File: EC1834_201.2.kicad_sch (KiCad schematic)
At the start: 69 parts, among them X4 Lautsprecher, X7 DB9_Female

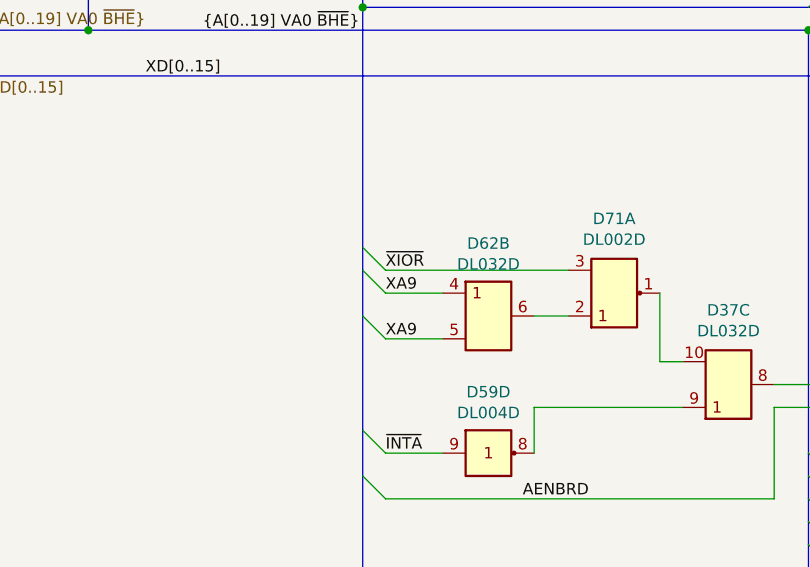
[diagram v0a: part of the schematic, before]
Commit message: Wrong Signal fixed
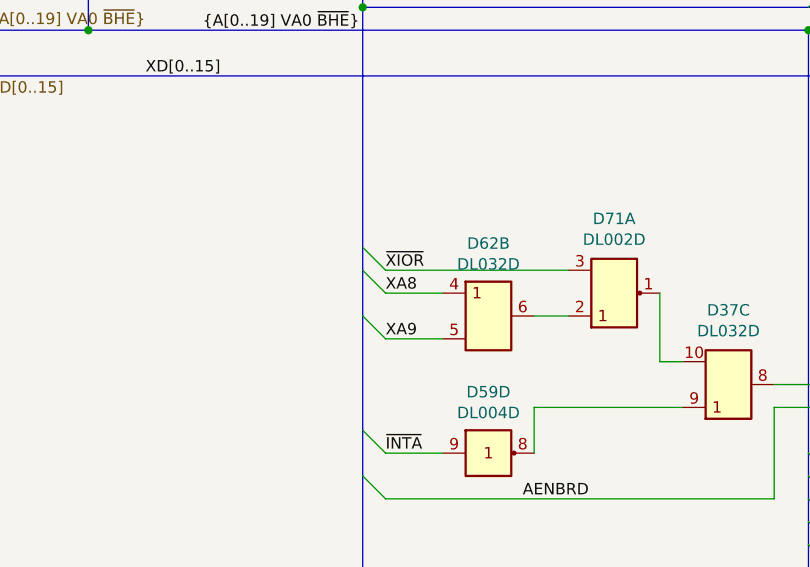
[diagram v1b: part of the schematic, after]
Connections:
- net XA8: now also D62.4 (A2)
- net XA9: no longer D62.4 (A2)
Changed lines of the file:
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@@
     (effects (font (size 1.27 1.27)) (justify left bottom))
   )
-  (label "XA9" (at 87.63 218.44 0)
+  (label "XA8" (at 87.63 218.44 0)
     (effects (font (size 1.27 1.27)) (justify left bottom))
   )

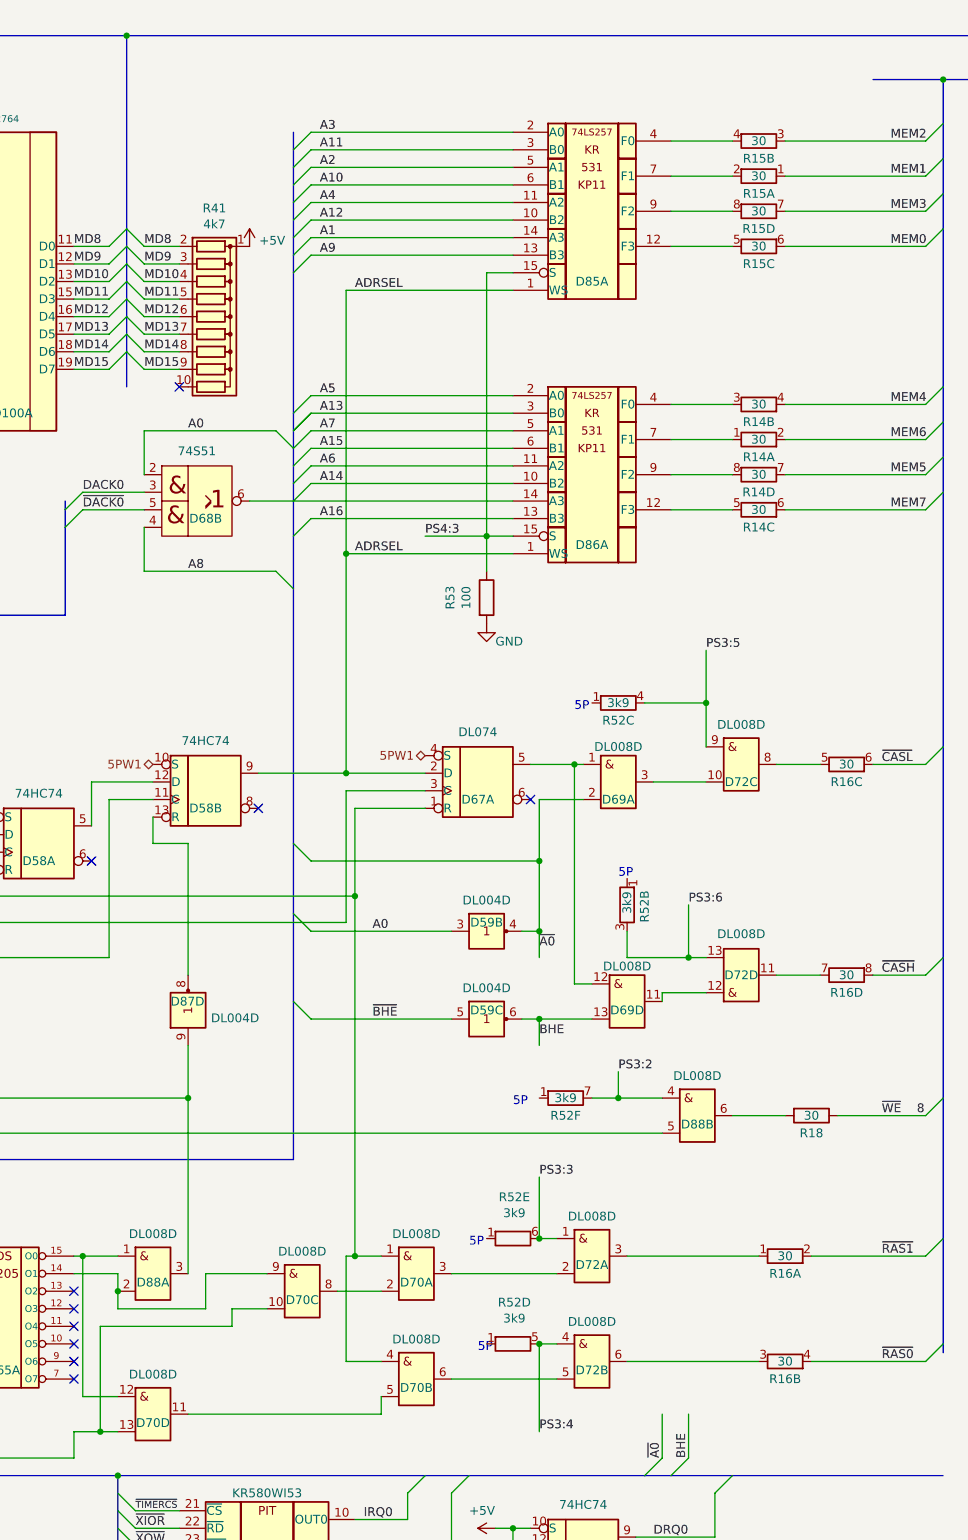
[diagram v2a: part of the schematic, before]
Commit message: Replaced/corrected D70 from DL008 with DL000 Updated schematics
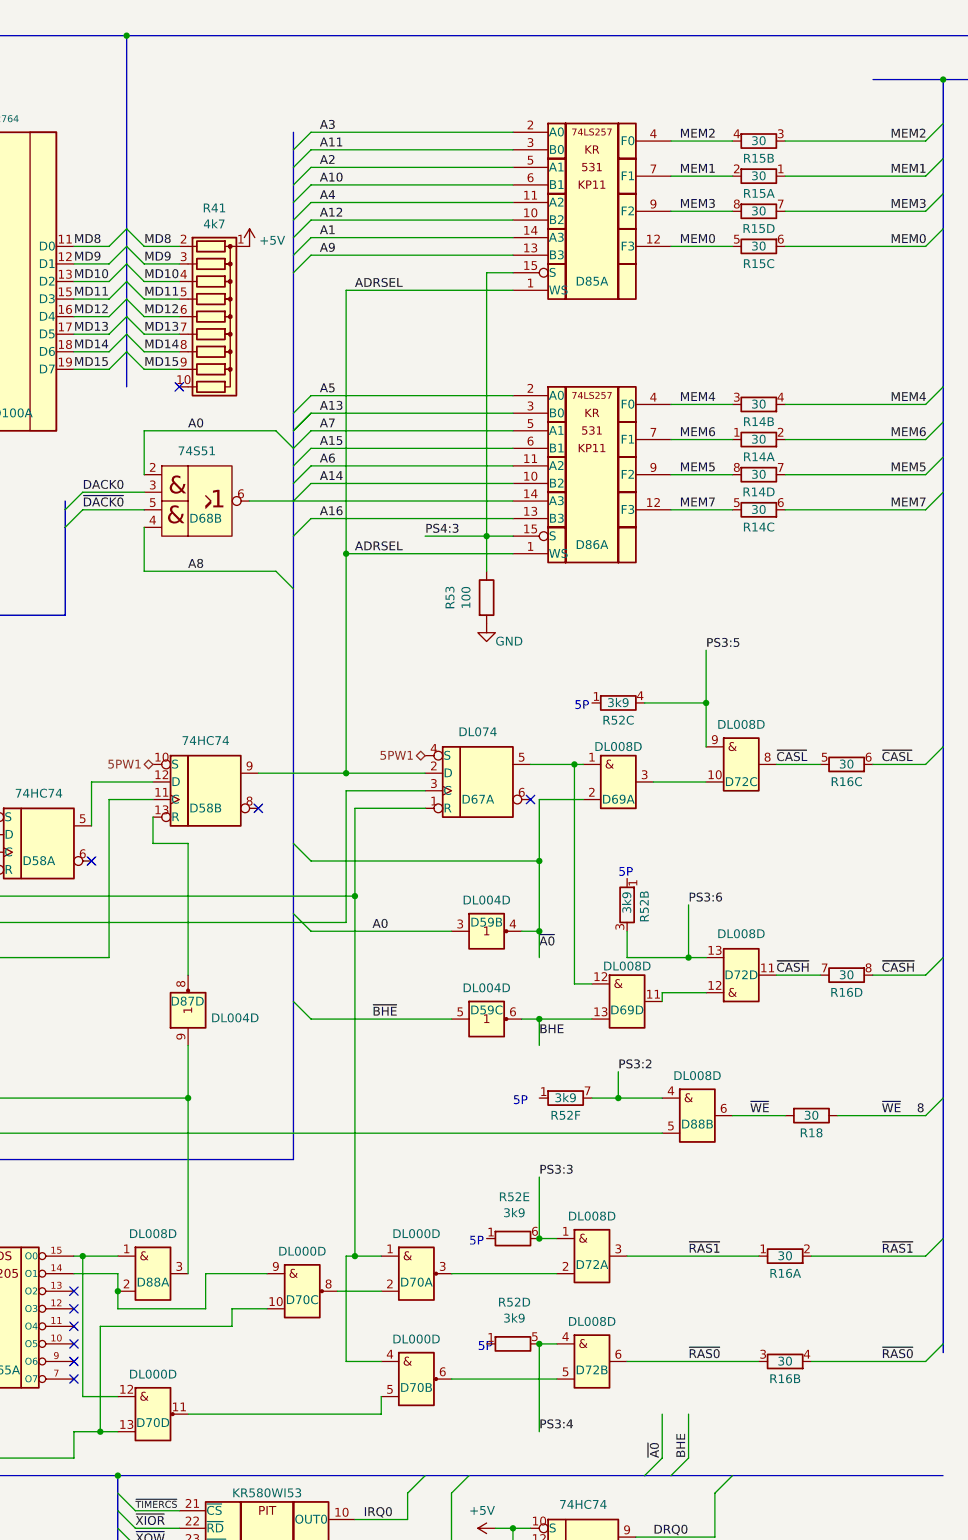
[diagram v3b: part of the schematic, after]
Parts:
- D70: value DL008D -> DL000D; symbol RFT_Digitalschaltkreise:DL008D -> robotron_ec1834:DL000D
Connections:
- net 8: now also D88.6 (Y2), R18.2
- net MEM0: now also D85.12 (F3), R15.5 (R3.1)
- net MEM1: now also D85.7 (F1), R15.2 (R1.2)
- net MEM2: now also D85.4 (F0), R15.4 (R2.2)
- net MEM3: now also D85.9 (F2), R15.8 (R4.2)
- net MEM4: now also D86.4 (F0), R14.3 (R2.1)
- net MEM5: now also D86.9 (F2), R14.8 (R4.2)
- net MEM6: now also D86.7 (F1), R14.1 (R1.1)
- net MEM7: now also D86.12 (F3), R14.5 (R3.1)
- net ~{CASH}: now also D72.11 (Y4), R16.7 (R4.1)
- net ~{CASL}: now also D72.8 (Y3), R16.5 (R3.1)
- net ~{RAS0}: now also D72.6 (Y2), R16.3 (R2.1)
- net ~{RAS1}: now also D72.3 (Y1), R16.1 (R1.1)
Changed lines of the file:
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@@
+    (effects (font (size 1.27 1.27)) (justify left bottom))
+  )
+  (label "MEM2" (at 344.17 41.91 0)
     (effects (font (size 1.27 1.27)) (justify left bottom))
   )
@@
     (effects (font (size 1.27 1.27)) (justify left bottom))
   )
+  (label "MEM4" (at 344.17 80.01 0)
+    (effects (font (size 1.27 1.27)) (justify left bottom))
+  )
   (label "MD11" (at 256.54 64.77 0)
     (effects (font (size 1.27 1.27)) (justify left bottom))
@@
     (effects (font (size 1.27 1.27)) (justify left bottom))
   )
+  (label "MEM5" (at 344.17 90.17 0)
+    (effects (font (size 1.27 1.27)) (justify left bottom))
+  )
   (label "MD13" (at 256.54 69.85 0)
     (effects (font (size 1.27 1.27)) (justify left bottom))
@@
     (effects (font (size 1.27 1.27)) (justify left bottom))
   )
+  (label "~{RAS0}" (at 345.44 218.44 0)
+    (effects (font (size 1.27 1.27)) (justify left bottom))
+  )
   (label "MD4" (at 195.58 67.31 0)
     (effects (font (size 1.27 1.27)) (justify left bottom))
@@
     (effects (font (size 1.27 1.27)) (justify left bottom))
   )
+  (label "MEM7" (at 344.17 95.25 0)
+    (effects (font (size 1.27 1.27)) (justify left bottom))
+  )
   (label "XA1" (at 189.23 288.29 0)
     (effects (font (size 1.27 1.27)) (justify left bottom))
@@
     (effects (font (size 1.27 1.27)) (justify left bottom))
   )
+  (label "MEM3" (at 344.17 52.07 0)
+    (effects (font (size 1.27 1.27)) (justify left bottom))
+  )
   (label "~{NMIREGCS}" (at 87.63 316.23 0)
     (effects (font (size 1.27 1.27)) (justify left bottom))
@@
     (effects (font (size 1.27 1.27)) (justify left bottom))
   )
+  (label "~{CASH}" (at 358.14 162.56 0)
+    (effects (font (size 1.27 1.27)) (justify left bottom))
+  )
   (label "D8" (at 142.24 143.51 0)
     (effects (font (size 1.27 1.27)) (justify left bottom))
@@
     (effects (font (size 1.27 1.27)) (justify left bottom))
   )
+  (label "~{WE}" (at 354.33 182.88 0)
+    (effects (font (size 1.27 1.27)) (justify left bottom))
+  )
   (label "XA5" (at 229.87 52.07 0)
     (effects (font (size 1.27 1.27)) (justify left bottom))
@@
     (effects (font (size 1.27 1.27)) (justify left bottom))
   )
+  (label "MEM0" (at 344.17 57.15 0)
+    (effects (font (size 1.27 1.27)) (justify left bottom))
+  )
   (label "MD15" (at 266.7 74.93 0)
     (effects (font (size 1.27 1.27)) (justify left bottom))
   )
+  (label "~{CASL}" (at 358.14 132.08 0)
+    (effects (font (size 1.27 1.27)) (justify left bottom))
+  )
   (label "PA7" (at 314.96 303.53 0)
     (effects (font (size 1.27 1.27)) (justify left bottom))
@@
     (effects (font (size 1.27 1.27)) (justify left bottom))
   )
+  (label "MEM6" (at 344.17 85.09 0)
+    (effects (font (size 1.27 1.27)) (justify left bottom))
+  )
   (label "MD14" (at 266.7 72.39 0)
     (effects (font (size 1.27 1.27)) (justify left bottom))
@@
   )
   (label "MD11" (at 167.64 151.13 0)
+    (effects (font (size 1.27 1.27)) (justify left bottom))
+  )
+  (label "~{RAS1}" (at 345.44 203.2 0)
     (effects (font (size 1.27 1.27)) (justify left bottom))
   )
@@
   )
   (label "~{XIOR}" (at 265.43 242.57 0)
+    (effects (font (size 1.27 1.27)) (justify left bottom))
+  )
+  (label "MEM1" (at 344.17 46.99 0)
     (effects (font (size 1.27 1.27)) (justify left bottom))
   )
@@
     (pin "7")
   )
-  (symbol (lib_id "RFT_Digitalschaltkreise:DL008D") (at 306.07 205.74 0) (unit 1)
+  (symbol (lib_id "robotron_ec1834:DL000D") (at 306.07 205.74 0) (unit 1)
     (in_bom yes) (on_board yes)
     (property "Reference" "D70" (id 0) (at 306.07 207.01 0))
-    (property "Value" "DL008D" (id 1) (at 306.07 199.9996 0))
+    (property "Value" "DL000D" (id 1) (at 306.07 199.9996 0))
     (property "Footprint" "Package_DIP:DIP-14_W7.62mm" (id 2) (at 306.07 205.74 0)
       (effects (font (size 1.27 1.27)) hide)
     )
-    (property "Datasheet" "https://www-user.tu-chemnitz.de/~heha/basteln/Konsumg%C3%BCter/DDR-Halbleiter/dl008.gif" (id 3) (at 306.07 205.74 0)
-      (effects (font (size 1.27 1.27)) hide)
-    )
-    (pin "3")
-    (pin "1")
-    (pin "2")
-    (pin "4")
-    (pin "5")
-    (pin "6")
-    (pin "8")
-    (pin "10")
-    (pin "9")
-    (pin "11")
-    (pin "12")
-    (pin "13")
-    (pin "14")
-    (pin "7")
-  )
-  (symbol (lib_id "RFT_Digitalschaltkreise:DL008D") (at 306.07 220.98 0) (unit 2)
+    (property "Datasheet" "https://www-user.tu-chemnitz.de/~heha/basteln/Konsumg%C3%BCter/DDR-Halbleiter/dl000.gif" (id 3) (at 306.07 213.36 0)
+      (effects (font (size 1.27 1.27)) hide)
+    )
+    (pin "3")
+    (pin "1")
+    (pin "2")
+    (pin "4")
+    (pin "5")
+    (pin "6")
+    (pin "8")
+    (pin "10")
+    (pin "9")
+    (pin "11")
+    (pin "12")
+    (pin "13")
+    (pin "14")
+    (pin "7")
+  )
+  (symbol (lib_id "robotron_ec1834:DL000D") (at 306.07 220.98 0) (unit 2)
     (in_bom yes) (on_board yes)
     (property "Reference" "D70" (id 0) (at 306.07 222.25 0))
-    (property "Value" "DL008D" (id 1) (at 306.07 215.2396 0))
+    (property "Value" "DL000D" (id 1) (at 306.07 215.2396 0))
     (property "Footprint" "Package_DIP:DIP-14_W7.62mm" (id 2) (at 306.07 220.98 0)
       (effects (font (size 1.27 1.27)) hide)
     )
-    (property "Datasheet" "https://www-user.tu-chemnitz.de/~heha/basteln/Konsumg%C3%BCter/DDR-Halbleiter/dl008.gif" (id 3) (at 306.07 220.98 0)
+    (property "Datasheet" "https://www-user.tu-chemnitz.de/~heha/basteln/Konsumg%C3%BCter/DDR-Halbleiter/dl000.gif" (id 3) (at 306.07 228.6 0)
       (effects (font (size 1.27 1.27)) hide)
     )
@@
     (pin "7")
   )
-  (symbol (lib_id "RFT_Digitalschaltkreise:DL008D") (at 267.97 226.06 0) (unit 4)
+  (symbol (lib_id "robotron_ec1834:DL000D") (at 267.97 226.06 0) (unit 4)
     (in_bom yes) (on_board yes)
     (property "Reference" "D70" (id 0) (at 267.97 227.33 0))
-    (property "Value" "DL008D" (id 1) (at 267.97 220.3196 0))
+    (property "Value" "DL000D" (id 1) (at 267.97 220.3196 0))
     (property "Footprint" "Package_DIP:DIP-14_W7.62mm" (id 2) (at 267.97 226.06 0)
       (effects (font (size 1.27 1.27)) hide)
     )
-    (property "Datasheet" "https://www-user.tu-chemnitz.de/~heha/basteln/Konsumg%C3%BCter/DDR-Halbleiter/dl008.gif" (id 3) (at 267.97 226.06 0)
-      (effects (font (size 1.27 1.27)) hide)
-    )
-    (pin "3")
-    (pin "1")
-    (pin "2")
-    (pin "4")
-    (pin "5")
-    (pin "6")
-    (pin "8")
-    (pin "10")
-    (pin "9")
-    (pin "11")
-    (pin "12")
-    (pin "13")
-    (pin "14")
-    (pin "7")
-  )
-  (symbol (lib_id "RFT_Digitalschaltkreise:DL008D") (at 289.56 208.28 0) (unit 3)
+    (property "Datasheet" "https://www-user.tu-chemnitz.de/~heha/basteln/Konsumg%C3%BCter/DDR-Halbleiter/dl000.gif" (id 3) (at 267.97 233.68 0)
+      (effects (font (size 1.27 1.27)) hide)
+    )
+    (pin "3")
+    (pin "1")
+    (pin "2")
+    (pin "4")
+    (pin "5")
+    (pin "6")
+    (pin "8")
+    (pin "10")
+    (pin "9")
+    (pin "11")
+    (pin "12")
+    (pin "13")
+    (pin "14")
+    (pin "7")
+  )
+  (symbol (lib_id "robotron_ec1834:DL000D") (at 289.56 208.28 0) (unit 3)
     (in_bom yes) (on_board yes)
     (property "Reference" "D70" (id 0) (at 289.56 209.55 0))
-    (property "Value" "DL008D" (id 1) (at 289.56 202.5396 0))
+    (property "Value" "DL000D" (id 1) (at 289.56 202.5396 0))
     (property "Footprint" "Package_DIP:DIP-14_W7.62mm" (id 2) (at 289.56 208.28 0)
       (effects (font (size 1.27 1.27)) hide)
     )
-    (property "Datasheet" "https://www-user.tu-chemnitz.de/~heha/basteln/Konsumg%C3%BCter/DDR-Halbleiter/dl008.gif" (id 3) (at 289.56 208.28 0)
-      (effects (font (size 1.27 1.27)) hide)
-    )
+    (property "Datasheet" "https://www-user.tu-chemnitz.de/~heha/basteln/Konsumg%C3%BCter/DDR-Halbleiter/dl000.gif" (id 3) (at 289.56 215.9 0)
+      (effects (font (size 1.27 1.27)) hide)
+    )
